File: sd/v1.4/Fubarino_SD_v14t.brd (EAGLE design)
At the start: 71.2 x 25.6 mm, 35 parts, among them IC1 PIC32MX440F256H-80I/PT, J8 UX60A-MB-5ST, Q1 8.000MHz, Q2 32.768 KHz

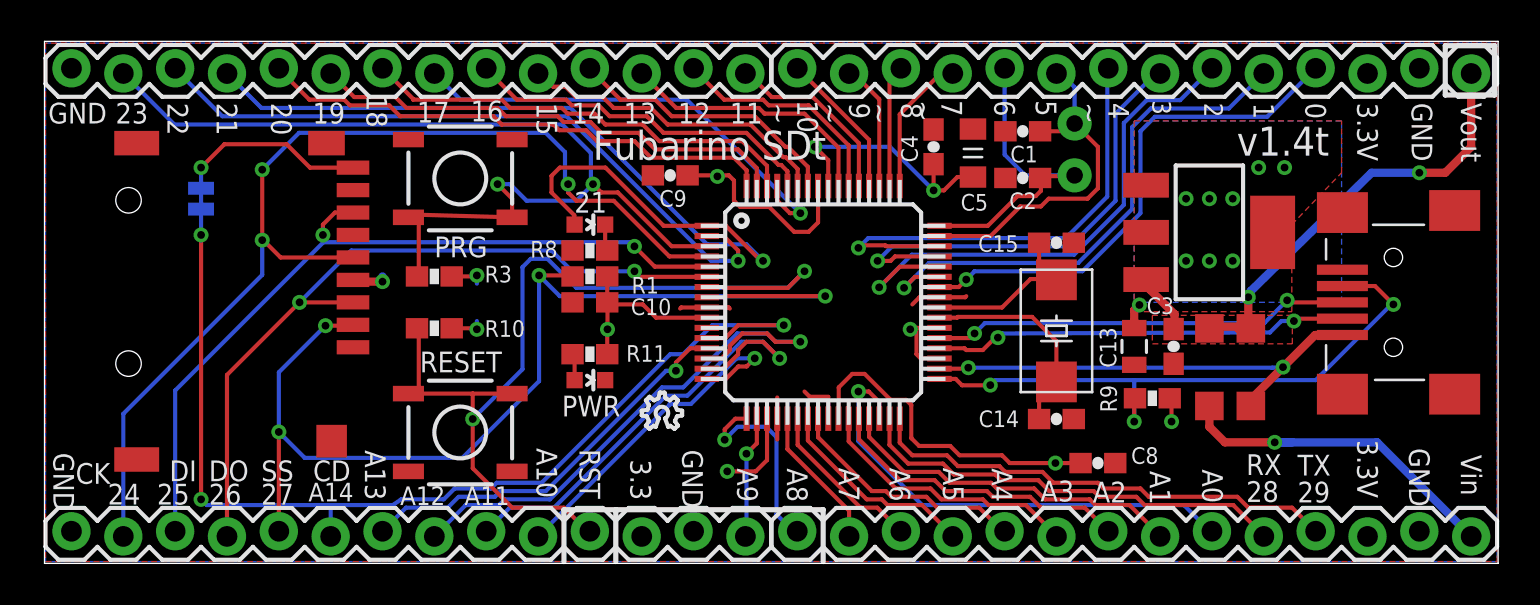
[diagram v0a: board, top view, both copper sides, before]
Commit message: Adjusted pads/holes for SD, buttons, and lock headers: cobra18t <https://github.com/cobra18t>
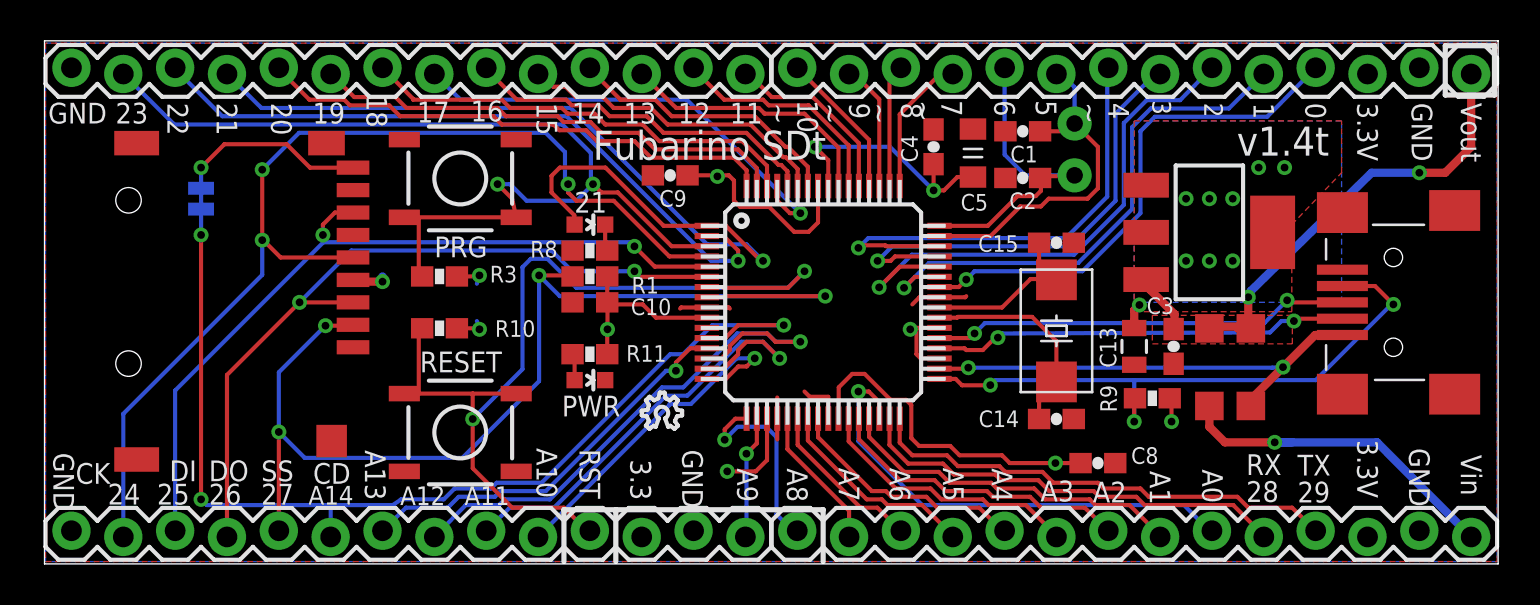
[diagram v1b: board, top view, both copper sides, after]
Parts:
- JP1, JP2, JP3, JP4: device SparkFun:1X14_LOCK -> TEF_made3:1X14_LOCK
- PROGRAM, RESET: device SparkFun02-20-08:TACTILE_SWITCH_SMD -> TEF_made3:TACTILE_SWITCH_SMD
- moved R10 0.25 mm to (19.3, 11.4)
- moved R3 0.25 mm to (19.3, 14.0)
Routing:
- net !MCLR!: track 47.7 -> 48.2 mm
